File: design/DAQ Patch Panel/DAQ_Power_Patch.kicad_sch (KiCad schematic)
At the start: 16 parts, among them J1 Screw_Terminal_01x05, J7 Sensor 1 Terminal, J8 Sensor 1 Output

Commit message: First Half of Changes
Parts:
- removed J8: Sensor 1 Output, TerminalBlock_Phoenix:TerminalBlock_Phoenix_MKDS-1,5-2-5.08_1x02_P5.08mm_Horizontal, symbol Connector:Screw_Terminal_01x02
- added J2: Screw_Terminal_01x06, symbol Connector:Screw_Terminal_01x06
- F1: value 50mA fuse -> 50mA
- R1, R5: value 10k -> 10k 1%
- R2, R6: value 100R -> 100R 1%
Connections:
- net +20V: now also JP1.4 (C); no longer JP1.3 (B)
- net +5V: now also JP1.3 (B); no longer JP1.4 (C)
- net DATA 1: now also J2.1 (Pin_1); no longer JP7.2 (C)
- net DATA 2: now also J2.2 (Pin_2); no longer JP2.2 (C)
- net POWER: now also JP1.2 (C)
- net at F1.1: no longer JP1.2 (C)
- net DATA 1 FILTER IN renamed IN 1
- net IN 1: now also JP7.2 (C)
- net DATA 2 FILTER IN renamed IN 2
- net IN 2: now also JP2.2 (C)
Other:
- moved on the sheet: C1, C2, F1, J1, JP2, JP7, R1, R2, R3, R4, R5, R6

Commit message: More Requested Changes
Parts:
- added J3: Power 2 Terminal, TerminalBlock_Phoenix:TerminalBlock_Phoenix_MKDS-1,5-5-5.08_1x05_P5.08mm_Horizontal, symbol Connector:Screw_Terminal_01x05
- C1: footprint Library:4-Pole Jumper -> Capacitor_SMD:C_0805_2012Metric_Pad1.18x1.45mm_HandSolder
- J1: value Screw_Terminal_01x05 -> Power 1 Terminal
- JP2, JP4, JP7: footprint Jumper:SolderJumper-3_P1.3mm_Open_RoundedPad1.0x1.5mm -> Connector_PinHeader_2.54mm:PinHeader_1x03_P2.54mm_Vertical
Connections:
- net +10V: now also J3.2 (Pin_2)
- net +12V: now also J3.3 (Pin_3)
- net +20V: now also J3.4 (Pin_4)
- net +5V: now also J3.1 (Pin_1)
- net GND: now also J3.5 (Pin_5)
- net POWER: now also F1.1; no longer F1.2, JP1.2 (C)
- new net: F1.2, JP1.2 (C)
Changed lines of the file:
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@@
   (junction (at 190.5 106.68) (diameter 0) (color 0 0 0 0)
   )
-  (junction (at 191.77 90.17) (diameter 0) (color 0 0 0 0)
-  )
   (wire (pts (xy 142.24 82.55) (xy 142.24 90.17))
     (stroke (width 0) (type default))
@@
   )
   (wire (pts (xy 120.65 49.53) (xy 120.65 63.5))
-    (stroke (width 0) (type default))
-  )
-  (wire (pts (xy 191.77 90.17) (xy 191.77 91.44))
     (stroke (width 0) (type default))
   )
@@
     (effects (font (size 1.27 1.27)) (justify right bottom))
   )
-  (label "POWER" (at 142.24 63.5 180) (fields_autoplaced)
-    (effects (font (size 1.27 1.27)) (justify right bottom))
+  (label "POWER" (at 152.4 63.5 0) (fields_autoplaced)
+    (effects (font (size 1.27 1.27)) (justify left bottom))
   )
   (label "DATA 1" (at 238.76 83.82 180) (fields_autoplaced)
@@
       (effects (font (size 1.27 1.27)) (justify left))
     )
-    (property "Footprint" "Library:4-Pole Jumper" (at 191.4652 115.57 0)
+    (property "Footprint" "Capacitor_SMD:C_0805_2012Metric_Pad1.18x1.45mm_HandSolder" (at 191.4652 115.57 0)
       (effects (font (size 1.27 1.27)) hide)
     )
@@
     )
   )
+  (symbol (lib_name "+10V_1") (lib_id "power:+10V") (at 72.39 58.42 270) (mirror x) (unit 1)
+    (in_bom yes) (on_board yes) (dnp no) (fields_autoplaced)
+    (property "Reference" "#PWR020" (at 68.58 58.42 0)
+      (effects (font (size 1.27 1.27)) hide)
+    )
+    (property "Value" "+20V" (at 76.2 58.42 90)
+      (effects (font (size 1.27 1.27)) (justify left))
+    )
+    (property "Footprint" "" (at 72.39 58.42 0)
+      (effects (font (size 1.27 1.27)) hide)
+    )
+    (property "Datasheet" "" (at 72.39 58.42 0)
+      (effects (font (size 1.27 1.27)) hide)
+    )
+    (pin "1")
+    (instances
+      (project "DAQ_Power_Patch"
+        (path "/da75d2ac-4c40-407d-8f74-3497a5ffc88d"
+          (reference "#PWR020") (unit 1)
+        )
+      )
+    )
+  )
   (symbol (lib_id "Device:C") (at 191.77 86.36 0) (unit 1)
     (in_bom yes) (on_board yes) (dnp no) (fields_autoplaced)
@@
         (path "/da75d2ac-4c40-407d-8f74-3497a5ffc88d"
           (reference "#PWR03") (unit 1)
+        )
+      )
+    )
+  )
+  (symbol (lib_id "power:+5V") (at 72.39 50.8 270) (mirror x) (unit 1)
+    (in_bom yes) (on_board yes) (dnp no) (fields_autoplaced)
+    (property "Reference" "#PWR015" (at 68.58 50.8 0)
+      (effects (font (size 1.27 1.27)) hide)
+    )
+    (property "Value" "+5V" (at 76.2 50.8 90)
+      (effects (font (size 1.27 1.27)) (justify left))
+    )
+    (property "Footprint" "" (at 72.39 50.8 0)
+      (effects (font (size 1.27 1.27)) hide)
+    )
+    (property "Datasheet" "" (at 72.39 50.8 0)
+      (effects (font (size 1.27 1.27)) hide)
+    )
+    (pin "1")
+    (instances
+      (project "DAQ_Power_Patch"
+        (path "/da75d2ac-4c40-407d-8f74-3497a5ffc88d"
+          (reference "#PWR015") (unit 1)
         )
       )
@@
     )
   )
+  (symbol (lib_id "power:+12V") (at 72.39 55.88 270) (mirror x) (unit 1)
+    (in_bom yes) (on_board yes) (dnp no) (fields_autoplaced)
+    (property "Reference" "#PWR019" (at 68.58 55.88 0)
+      (effects (font (size 1.27 1.27)) hide)
+    )
+    (property "Value" "+12V" (at 76.2 55.88 90)
+      (effects (font (size 1.27 1.27)) (justify left))
+    )
+    (property "Footprint" "" (at 72.39 55.88 0)
+      (effects (font (size 1.27 1.27)) hide)
+    )
+    (property "Datasheet" "" (at 72.39 55.88 0)
+      (effects (font (size 1.27 1.27)) hide)
+    )
+    (pin "1")
+    (instances
+      (project "DAQ_Power_Patch"
+        (path "/da75d2ac-4c40-407d-8f74-3497a5ffc88d"
+          (reference "#PWR019") (unit 1)
+        )
+      )
+    )
+  )
   (symbol (lib_name "Jumper_3_Open_1") (lib_id "Jumper:Jumper_3_Open") (at 148.59 82.55 180) (unit 1)
     (in_bom yes) (on_board yes) (dnp no)
@@
       (effects (font (size 1.27 1.27)) (justify left))
     )
-    (property "Footprint" "Jumper:SolderJumper-3_P1.3mm_Open_RoundedPad1.0x1.5mm" (at 148.59 82.55 0)
+    (property "Footprint" "Connector_PinHeader_2.54mm:PinHeader_1x03_P2.54mm_Vertical" (at 148.59 82.55 0)
       (effects (font (size 1.27 1.27)) hide)
     )
@@
   )
   (symbol (lib_id "Connector:Screw_Terminal_01x05") (at 67.31 72.39 0) (mirror y) (unit 1)
-    (in_bom yes) (on_board yes) (dnp no) (fields_autoplaced)
-    (property "Reference" "J1" (at 64.77 71.12 0)
-      (effects (font (size 1.27 1.27)) (justify left))
-    )
-    (property "Value" "Screw_Terminal_01x05" (at 64.77 73.66 0)
-      (effects (font (size 1.27 1.27)) (justify left))
+    (in_bom yes) (on_board yes) (dnp no)
+    (property "Reference" "J1" (at 55.88 69.85 0)
+      (effects (font (size 1.27 1.27)))
+    )
+    (property "Value" "Power 1 Terminal" (at 55.88 72.39 0)
+      (effects (font (size 1.27 1.27)))
     )
     (property "Footprint" "TerminalBlock_Phoenix:TerminalBlock_Phoenix_MKDS-1,5-5-5.08_1x05_P5.08mm_Horizontal" (at 67.31 72.39 0)
@@
     )
   )
+  (symbol (lib_id "power:GND") (at 72.39 60.96 90) (mirror x) (unit 1)
+    (in_bom yes) (on_board yes) (dnp no) (fields_autoplaced)
+    (property "Reference" "#PWR021" (at 78.74 60.96 0)
+      (effects (font (size 1.27 1.27)) hide)
+    )
+    (property "Value" "GND" (at 76.2 60.96 90)
+      (effects (font (size 1.27 1.27)) (justify right))
+    )
+    (property "Footprint" "" (at 72.39 60.96 0)
+      (effects (font (size 1.27 1.27)) hide)
+    )
+    (property "Datasheet" "" (at 72.39 60.96 0)
+      (effects (font (size 1.27 1.27)) hide)
+    )
+    (pin "1")
+    (instances
+      (project "DAQ_Power_Patch"
+        (path "/da75d2ac-4c40-407d-8f74-3497a5ffc88d"
+          (reference "#PWR021") (unit 1)
+        )
+      )
+    )
+  )
   (symbol (lib_id "Device:R_US") (at 119.38 92.71 0) (unit 1)
     (in_bom yes) (on_board yes) (dnp no)
@@
     )
   )
+  (symbol (lib_id "Connector:Screw_Terminal_01x05") (at 67.31 55.88 0) (mirror y) (unit 1)
+    (in_bom yes) (on_board yes) (dnp no)
+    (property "Reference" "J3" (at 55.88 53.34 0)
+      (effects (font (size 1.27 1.27)))
+    )
+    (property "Value" "Power 2 Terminal" (at 55.88 55.88 0)
+      (effects (font (size 1.27 1.27)))
+    )
+    (property "Footprint" "TerminalBlock_Phoenix:TerminalBlock_Phoenix_MKDS-1,5-5-5.08_1x05_P5.08mm_Horizontal" (at 67.31 55.88 0)
+      (effects (font (size 1.27 1.27)) hide)
+    )
+    (property "Datasheet" "~" (at 67.31 55.88 0)
+      (effects (font (size 1.27 1.27)) hide)
+    )
+    (pin "1")
+    (pin "2")
+    (pin "3")
+    (pin "4")
+    (pin "5")
+    (instances
+      (project "DAQ_Power_Patch"
+        (path "/da75d2ac-4c40-407d-8f74-3497a5ffc88d"
+          (reference "J3") (unit 1)
+        )
+      )
+    )
+  )
   (symbol (lib_name "Jumper_3_Open_1") (lib_id "Jumper:Jumper_3_Open") (at 96.52 133.35 270) (unit 1)
     (in_bom yes) (on_board yes) (dnp no) (fields_autoplaced)
@@
       (effects (font (size 1.27 1.27)) (justify left))
     )
-    (property "Footprint" "Jumper:SolderJumper-3_P1.3mm_Open_RoundedPad1.0x1.5mm" (at 96.52 133.35 0)
+    (property "Footprint" "Connector_PinHeader_2.54mm:PinHeader_1x03_P2.54mm_Vertical" (at 96.52 133.35 0)
       (effects (font (size 1.27 1.27)) hide)
     )
@@
       (effects (font (size 1.27 1.27)) (justify left))
     )
-    (property "Footprint" "Jumper:SolderJumper-3_P1.3mm_Open_RoundedPad1.0x1.5mm" (at 113.03 81.28 0)
+    (property "Footprint" "Connector_PinHeader_2.54mm:PinHeader_1x03_P2.54mm_Vertical" (at 113.03 81.28 0)
       (effects (font (size 1.27 1.27)) hide)
     )
@@
         )
       )
+    )
+  )
+  (symbol (lib_id "power:+10V") (at 72.39 53.34 270) (mirror x) (unit 1)
+    (in_bom yes) (on_board yes) (dnp no) (fields_autoplaced)
+    (property "Reference" "#PWR017" (at 68.58 53.34 0)
+      (effects (font (size 1.27 1.27)) hide)
+    )
+    (property "Value" "+10V" (at 76.2 53.34 90)
+      (effects (font (size 1.27 1.27)) (justify left))
+    )
+    (property "Footprint" "" (at 72.39 53.34 0)
+      (effects (font (size 1.27 1.27)) hide)
+    )
+    (property "Datasheet" "" (at 72.39 53.34 0)
+      (effects (font (size 1.27 1.27)) hide)
+    )
+    (pin "1")
+    (instances
+      (project "DAQ_Power_Patch"
+        (path "/da75d2ac-4c40-407d-8f74-3497a5ffc88d"
+          (reference "#PWR017") (unit 1)
+        )
+      )

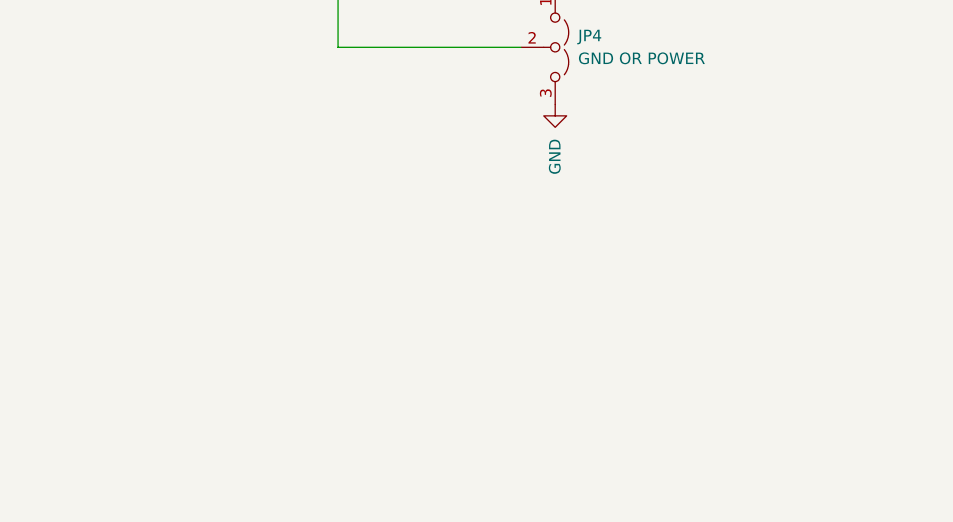
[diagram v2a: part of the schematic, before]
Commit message: 12 Pole Board Connector
Schematic Symbol and footprint for the 12 pole board connector created
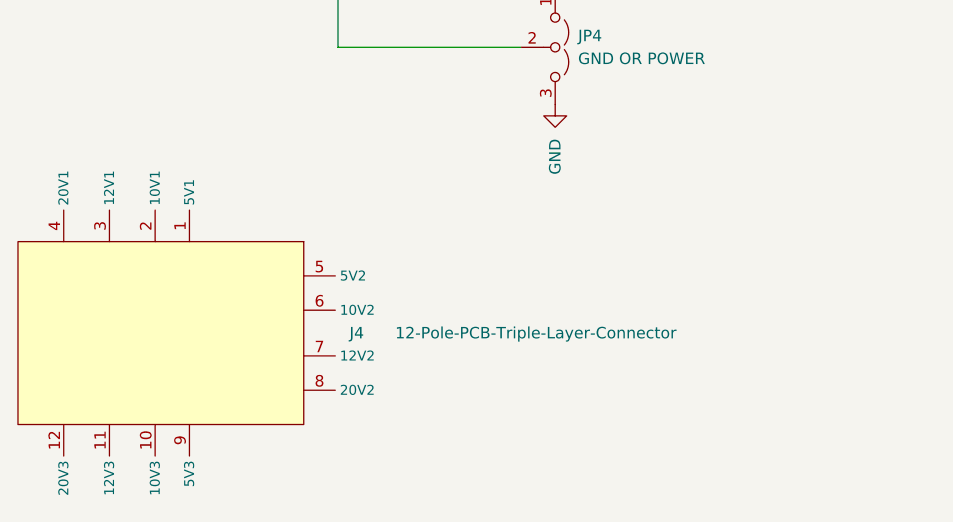
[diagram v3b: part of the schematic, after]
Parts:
- added J4: 12-Pole-PCB-Triple-Layer-Connector, Library:Weidmuller LM3RZF, symbol DAQLibrary:12-Pole-PCB-Triple-Layer-Connector
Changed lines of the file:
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@@
+    )
+  )
+  (symbol (lib_name "+10V_1") (lib_id "power:+10V") (at 72.39 74.93 270) (mirror x) (unit 1)
+    (in_bom yes) (on_board yes) (dnp no) (fields_autoplaced)
+    (property "Reference" "#PWR013" (at 68.58 74.93 0)
+      (effects (font (size 1.27 1.27)) hide)
+    )
+    (property "Value" "+20V" (at 76.2 74.93 90)
+      (effects (font (size 1.27 1.27)) (justify left))
+    )
+    (property "Footprint" "" (at 72.39 74.93 0)
+      (effects (font (size 1.27 1.27)) hide)
+    )
+    (property "Datasheet" "" (at 72.39 74.93 0)
+      (effects (font (size 1.27 1.27)) hide)
+    )
+    (pin "1")
+    (instances
+      (project "DAQ_Power_Patch"
+        (path "/da75d2ac-4c40-407d-8f74-3497a5ffc88d"
+          (reference "#PWR013") (unit 1)
+        )
+      )
     )
   )
@@
     )
   )
+  (symbol (lib_id "DAQLibrary:12-Pole-PCB-Triple-Layer-Connector") (at 54.61 165.1 270) (unit 1)
+    (in_bom yes) (on_board yes) (dnp no)
+    (property "Reference" "J4" (at 73.66 165.1 90)
+      (effects (font (size 1.27 1.27)) (justify left))
+    )
+    (property "Value" "12-Pole-PCB-Triple-Layer-Connector" (at 78.74 165.1 90)
+      (effects (font (size 1.27 1.27)) (justify left))
+    )
+    (property "Footprint" "Library:Weidmuller LM3RZF" (at 31.75 166.37 0)
+      (effects (font (size 1.27 1.27)) hide)
+    )
+    (property "Datasheet" "" (at 31.75 166.37 0)
+      (effects (font (size 1.27 1.27)) hide)
+    )
+    (pin "1")
+    (pin "10")
+    (pin "11")
+    (pin "12")
+    (pin "2")
+    (pin "3")
+    (pin "4")
+    (pin "5")
+    (pin "6")
+    (pin "7")
+    (pin "8")
+    (pin "9")
+    (instances
+      (project "DAQ_Power_Patch"
+        (path "/da75d2ac-4c40-407d-8f74-3497a5ffc88d"
+          (reference "J4") (unit 1)
+        )
+      )
+    )
+  )
   (symbol (lib_id "Device:R_US") (at 182.88 106.68 90) (unit 1)
     (in_bom yes) (on_board yes) (dnp no)
@@
         )
       )
-    )
-  )
-  (symbol (lib_name "+10V_1") (lib_id "power:+10V") (at 72.39 74.93 270) (mirror x) (unit 1)
-    (in_bom yes) (on_board yes) (dnp no) (fields_autoplaced)
-    (property "Reference" "#PWR013" (at 68.58 74.93 0)
-      (effects (font (size 1.27 1.27)) hide)
-    )
-    (property "Value" "+20V" (at 76.2 74.93 90)
-      (effects (font (size 1.27 1.27)) (justify left))
-    )
-    (property "Footprint" "" (at 72.39 74.93 0)
-      (effects (font (size 1.27 1.27)) hide)
-    )
-    (property "Datasheet" "" (at 72.39 74.93 0)
-      (effects (font (size 1.27 1.27)) hide)
-    )
-    (pin "1")
-    (instances
-      (project "DAQ_Power_Patch"
-        (path "/da75d2ac-4c40-407d-8f74-3497a5ffc88d"
-          (reference "#PWR013") (unit 1)
-        )
-      )
